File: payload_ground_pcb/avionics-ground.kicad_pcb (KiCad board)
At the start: 2 copper layers, 7 parts, among them J1 Micro_SD_Card, J2 Conn_Coaxial, SW1 SW_Push, U2 RFM95W-915S2, U3 NHD-0420H1Z, U5 LT1129-5.0_SOT223, U6 LT1129-3.3_SOT223

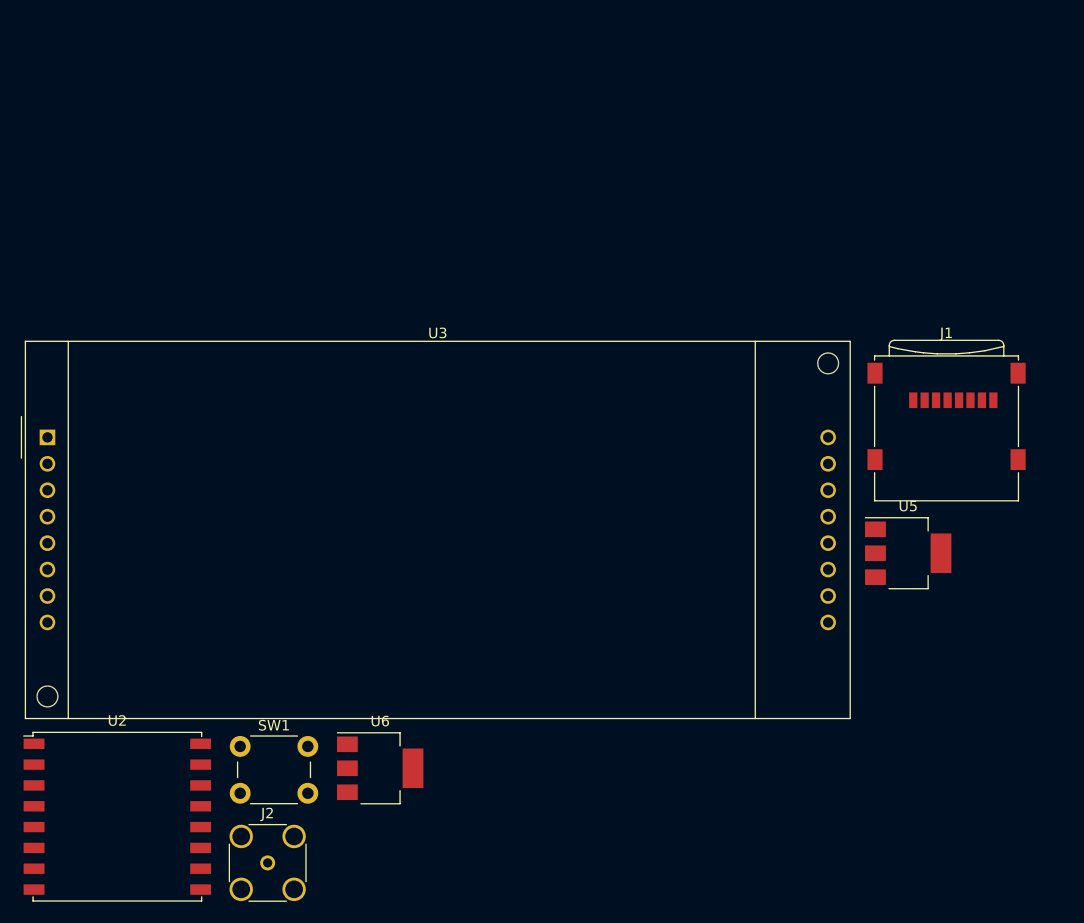
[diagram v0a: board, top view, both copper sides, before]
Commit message: Wired boards using autorouter
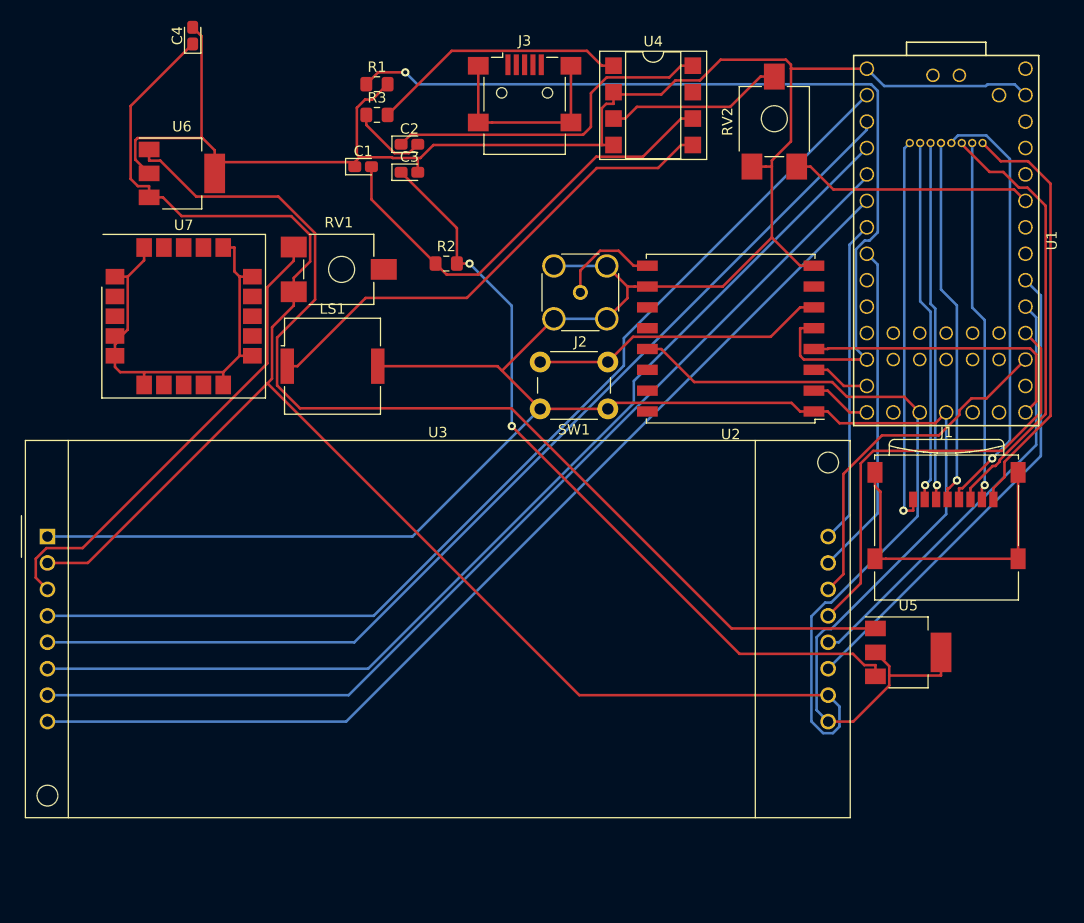
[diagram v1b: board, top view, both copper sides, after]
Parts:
- added C1: CP1_Small, Capacitor_Tantalum_SMD:CP_EIA-1608-08_AVX-J_Pad1.25x1.05mm_HandSolder, F.Cu at (88.1, 28.5)
- added C2: CP1_Small, Capacitor_Tantalum_SMD:CP_EIA-1608-08_AVX-J_Pad1.25x1.05mm_HandSolder, F.Cu at (92.6, 26.3)
- added C3: 3.3uF, Capacitor_Tantalum_SMD:CP_EIA-1608-08_AVX-J_Pad1.25x1.05mm_HandSolder, F.Cu at (92.6, 29.0)
- added C4: 3.3uF, Capacitor_Tantalum_SMD:CP_EIA-1608-08_AVX-J_Pad1.25x1.05mm_HandSolder, F.Cu at (71.8, 15.9)
- added J3: USB_B_Micro, Connector_USB:USB_Mini-B_Lumberg_2486_01_Horizontal, F.Cu at (103.6, 21.4)
- added LS1: Speaker, Buzzer_Beeper:Buzzer_Murata_PKMCS0909E4000-R1, F.Cu at (85.2, 47.6)
- added R1: R, Resistor_SMD:R_0805_2012Metric_Pad1.15x1.40mm_HandSolder, F.Cu at (89.5, 20.5)
- added R2: R, Resistor_SMD:R_0805_2012Metric_Pad1.15x1.40mm_HandSolder, F.Cu at (96.1, 37.8)
- added R3: R, Resistor_SMD:R_0805_2012Metric_Pad1.15x1.40mm_HandSolder, F.Cu at (89.5, 23.5)
- added RV1: R_POT, Potentiometer_SMD:Potentiometer_ACP_CA6-VSMD_Vertical_Hole, F.Cu at (85.8, 38.3)
- added RV2: R_POT, Potentiometer_SMD:Potentiometer_ACP_CA6-VSMD_Vertical_Hole, F.Cu at (127.6, 24.1)
- added U1: Teensy4.0, footprints:Teensy40, F.Cu at (144.1, 35.6)
- added U4: LM386, Package_DIP:DIP-8_W7.62mm_SMDSocket_SmallPads, F.Cu at (116.0, 22.6)
- added U7: ublox_SAM-M8Q, RF_GPS:ublox_SAM-M8Q, F.Cu at (70.9, 42.8)
- moved U2 74.7 mm to (123.4, 45.0), turned to 180 degrees
- moved J2 62.5 mm to (109.0, 40.5), turned to 180 degrees
- moved U6 60.2 mm to (70.7, 29.1)
- moved SW1 48.0 mm to (111.6, 51.7), turned to 180 degrees
- moved J1 9.52 mm to (144.2, 62.0)
- moved U3 9.52 mm to (57.8, 64.0)
- moved U5 9.52 mm to (140.5, 75.1)
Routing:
- net GND: track 0.00 -> 351.4 mm
- net +3V3: track 0.00 -> 216.0 mm
- net +BATT: track 0.00 -> 103.2 mm
- net RS: track 0.00 -> 101.0 mm
- net E: track 0.00 -> 100.7 mm
- net RW: track 0.00 -> 99.9 mm
- net DB0: track 0.00 -> 99.6 mm
- net DB1: track 0.00 -> 99.4 mm
- net CS: track 0.00 -> 88.3 mm, vias 0 -> 1
- net +5V: track 0.00 -> 75.0 mm, vias 0 -> 2
- net Net-(LS1-Pad1): track 0.00 -> 47.8 mm
- net DB7: track 0.00 -> 46.4 mm
- net Net-(RV1-Pad3): track 0.00 -> 45.7 mm
- net Net-(U7-Pad1): track 0.00 -> 43.8 mm
- net DB5: track 0.00 -> 43.5 mm
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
